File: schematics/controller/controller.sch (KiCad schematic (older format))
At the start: 10 parts

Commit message: PDF render
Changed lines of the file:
@@
 F0 "cpu" 60
 F1 "sub_assy/cpu.sch" 60
+F2 "V_LOGIC" U L 10400 6100 60
+F3 "GND" U L 10400 6200 60
+F4 "SDA_10" B R 12650 5400 60
+F5 "SCL_10" B R 12650 5500 60
+F6 "SDA_HIBAUD" B R 12650 5800 60
+F7 "SCL_HIBAUD" B R 12650 5900 60
+F8 "RESET" I L 10400 5400 60
 $EndSheet
 $EndSCHEMATC

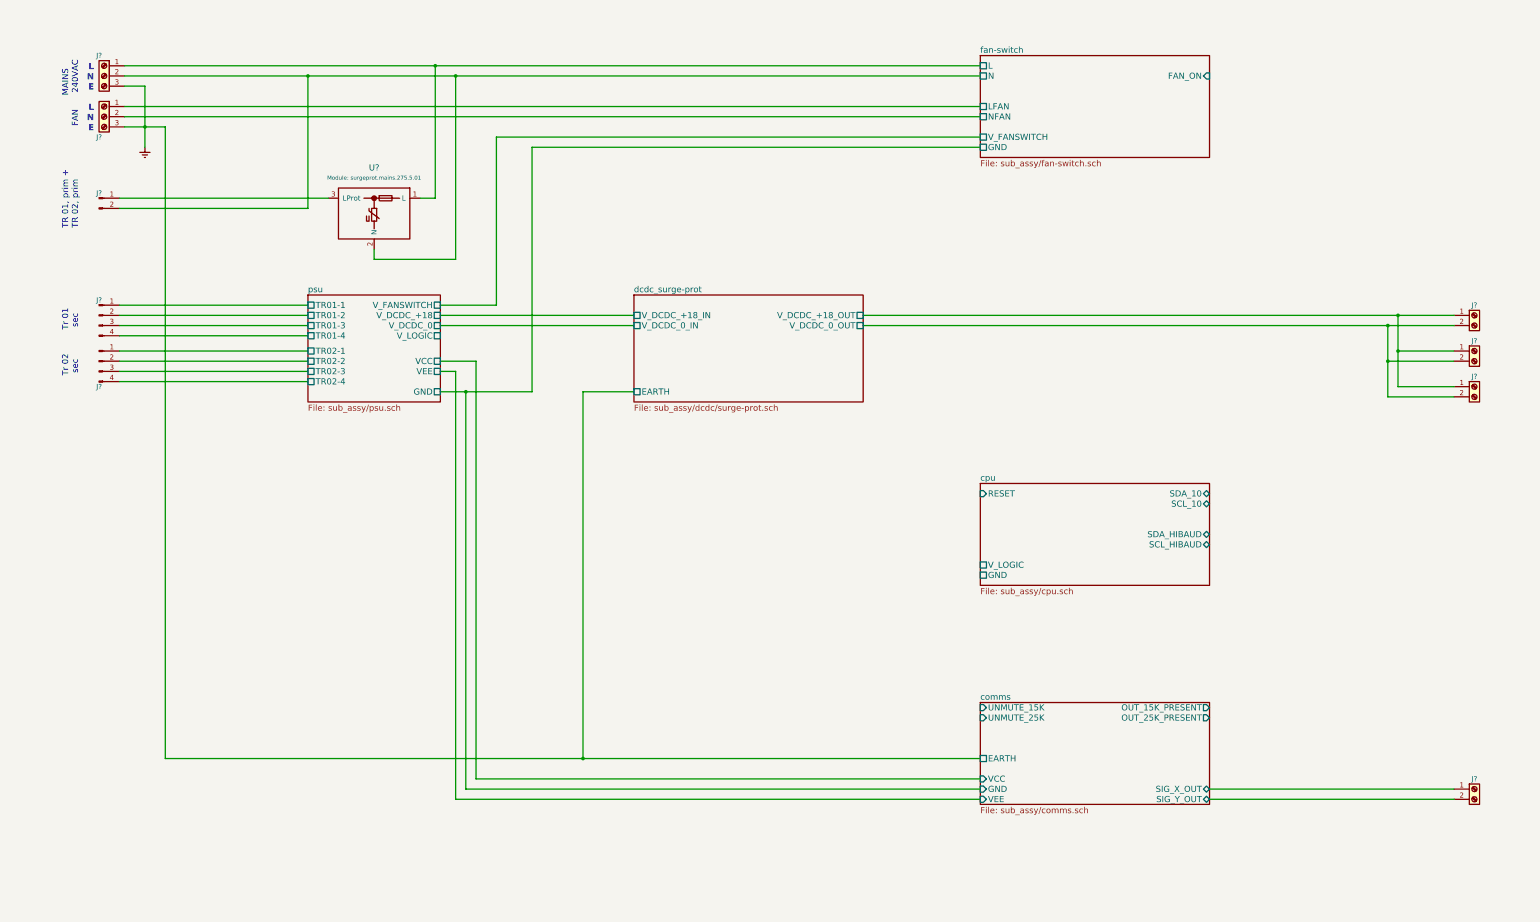
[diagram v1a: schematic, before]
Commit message: Developing and integrating comms i/o router.
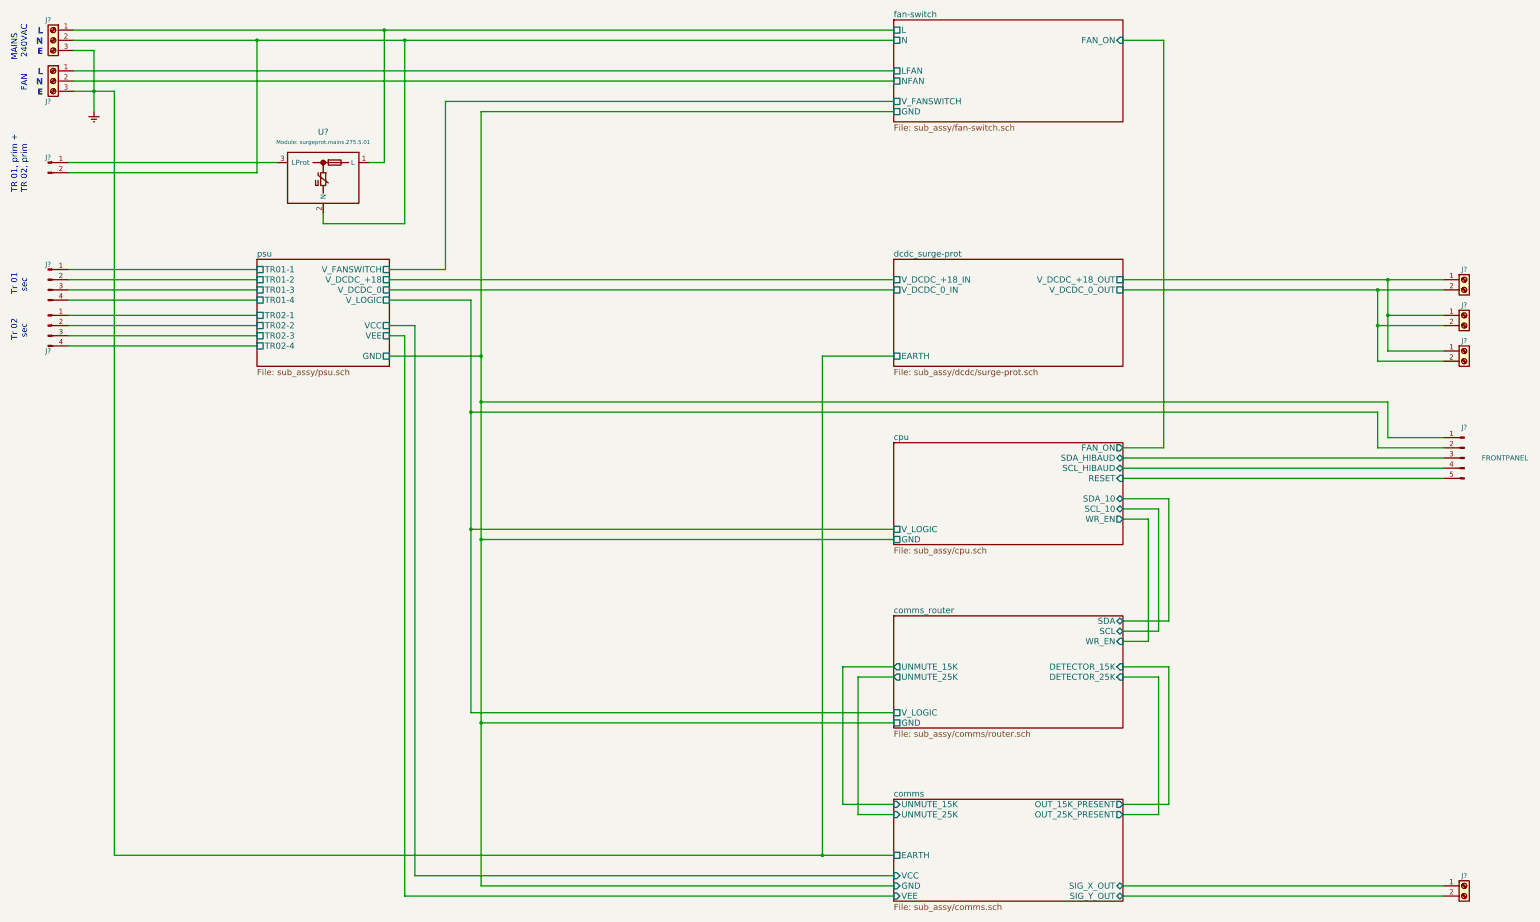
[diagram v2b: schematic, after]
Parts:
- added J?: FRONTPANEL, symbol Conn_01x05_Male
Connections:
- net comms/GND: now also J?.1 (Pin_1)
- net cpu/RESET: now also J?.5 (Pin_5)
- net cpu/SCL_HIBAUD: now also J?.4 (Pin_4)
- net cpu/SDA_HIBAUD: now also J?.3 (Pin_3)
- new net comms_router/V_LOGIC: J?.2 (Pin_2)
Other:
- moved on the sheet: J?, U?

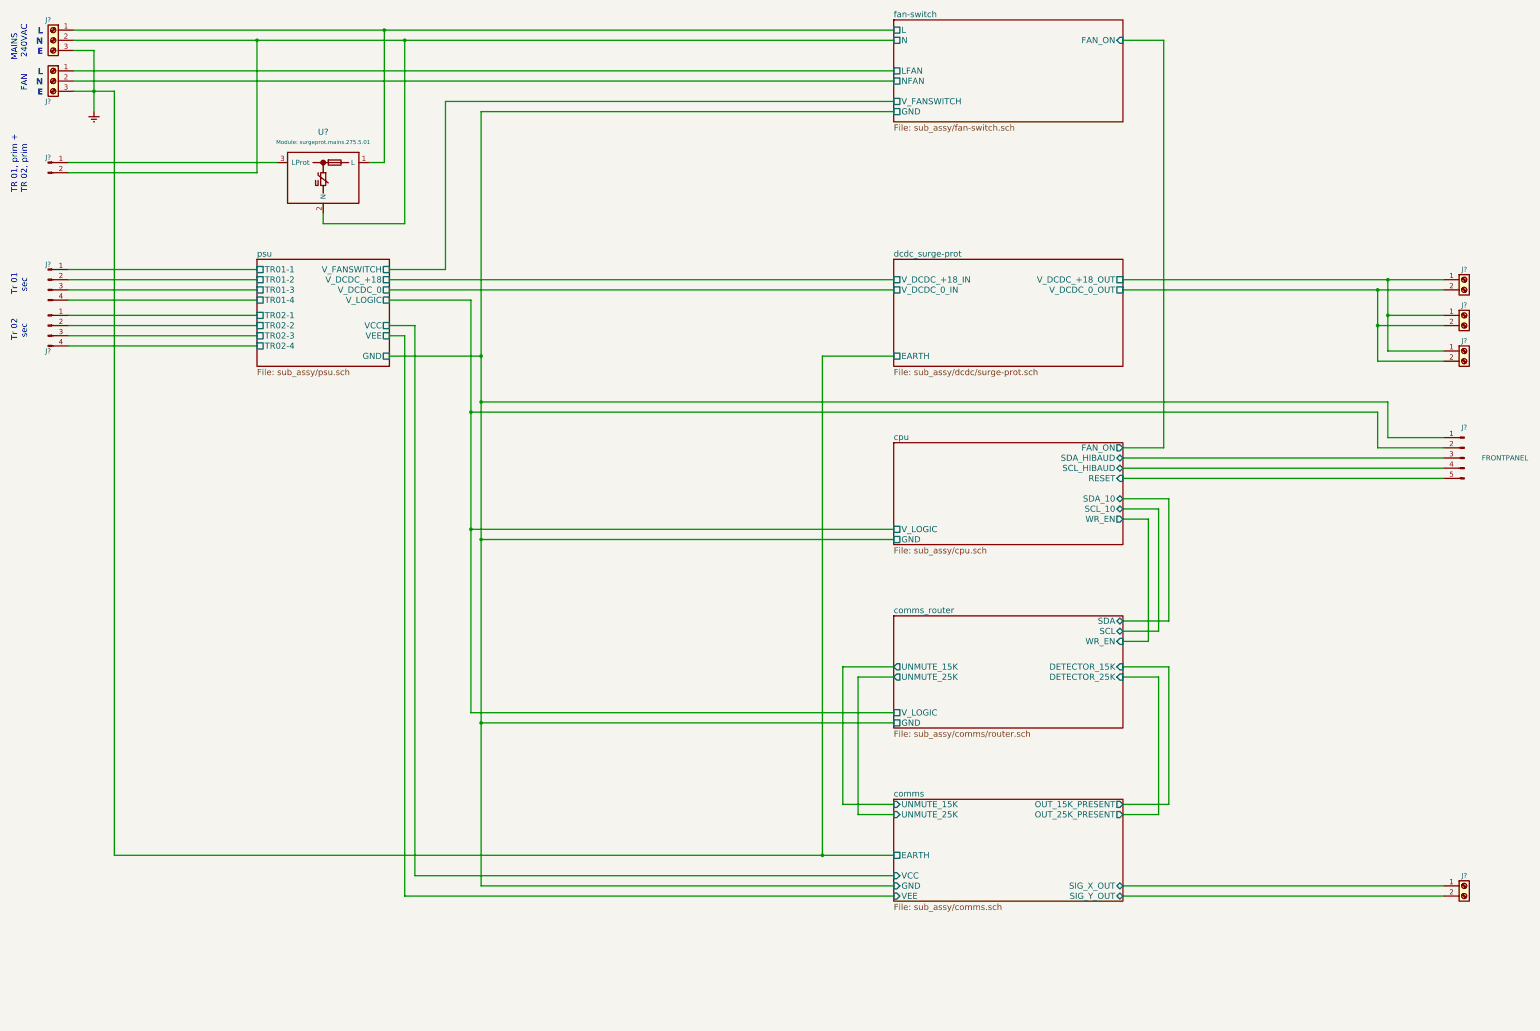
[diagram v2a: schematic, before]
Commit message: Annotation and DRC rule check
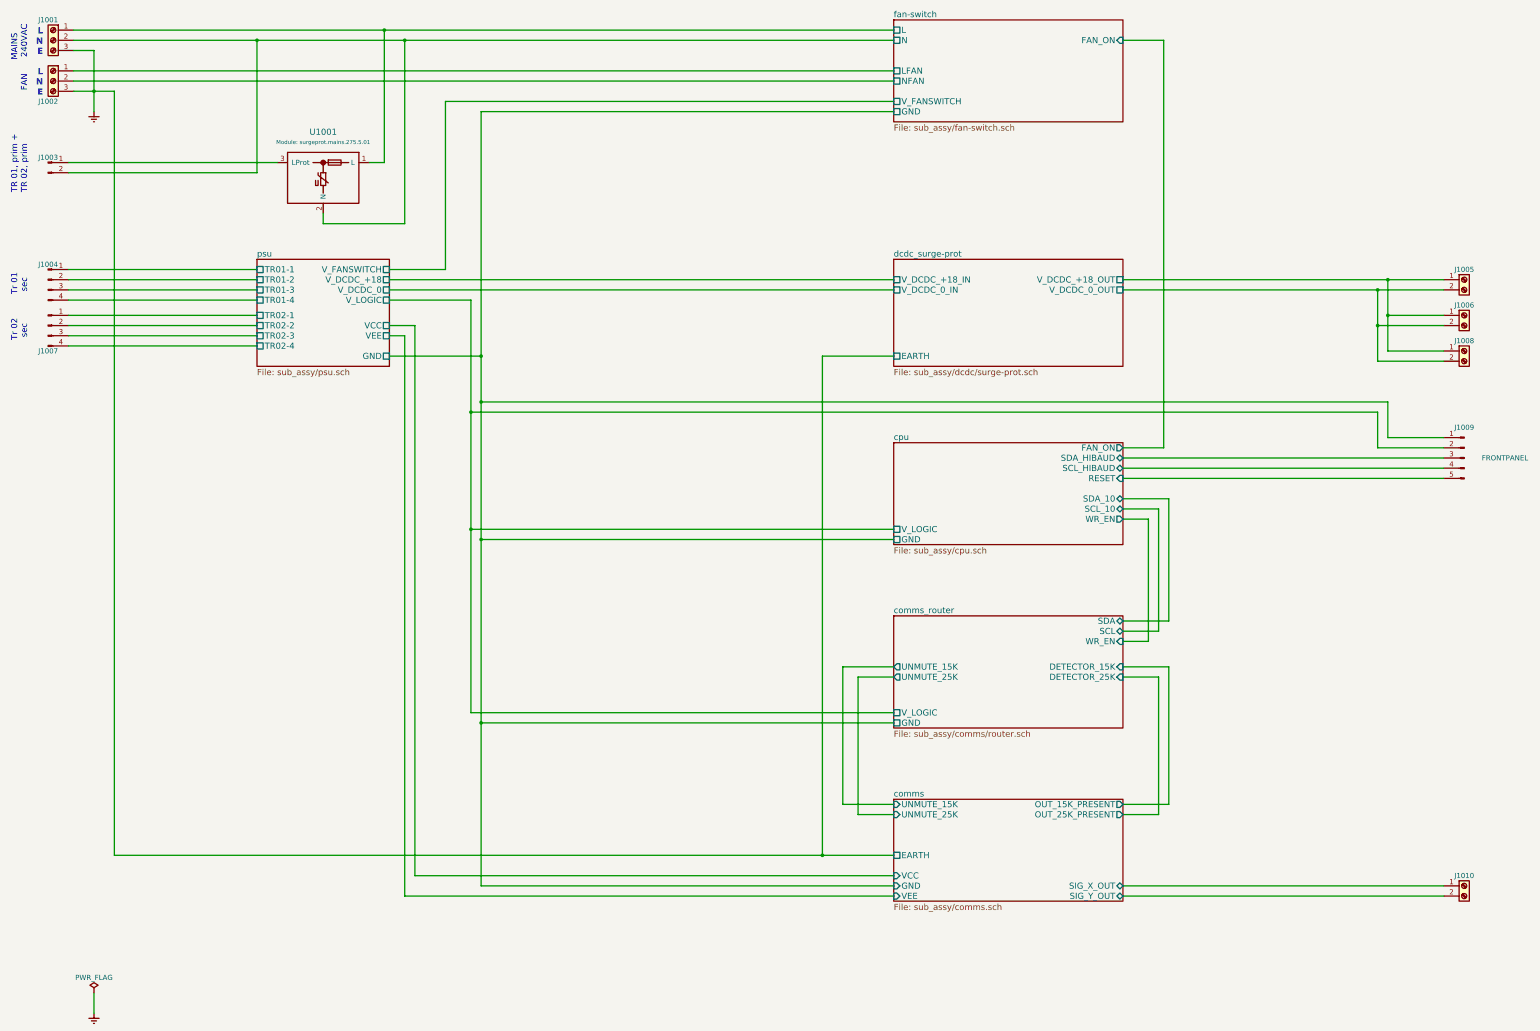
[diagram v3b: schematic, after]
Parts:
- gave numbers to parts that had none: 11
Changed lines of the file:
@@
 $EndSheet
 $Comp
-L Conn_01x04_Male J?
+L Conn_01x04_Male J1004
 U 1 1 59D2E43C
 P 1250 3300
-F 0 "J?" H 1250 3450 50  0000 C CNN
+F 0 "J1004" H 1250 3450 50  0000 C CNN
 F 1 "Conn_01x04_Male" H 1250 3000 50  0001 C CNN
 F 2 "" H 1250 3300 50  0001 C CNN
@@
 $EndComp
 $Comp
-L Conn_01x04_Male J?
+L Conn_01x04_Male J1007
 U 1 1 59D2EA34
 P 1250 3750
-F 0 "J?" H 1250 3500 50  0000 C CNN
+F 0 "J1007" H 1250 3500 50  0000 C CNN
 F 1 "Conn_01x04_Male" H 1250 3450 50  0001 C CNN
 F 2 "" H 1250 3750 50  0001 C CNN
@@
 $EndComp
 $Comp
-L Screw_Terminal_01x03 J?
+L Screw_Terminal_01x03 J1001
 U 1 1 59D41362
 P 1300 950
-F 0 "J?" H 1350 1150 50  0000 C CNN
+F 0 "J1001" H 1350 1150 50  0000 C CNN
 F 1 "Screw_Terminal_01x03" H 1300 750 50  0001 C CNN
 F 2 "" H 1300 950 50  0001 C CNN
@@
 $EndComp
 $Comp
-L Screw_Terminal_01x03 J?
+L Screw_Terminal_01x03 J1002
 U 1 1 59D44A54
 P 1300 1350
-F 0 "J?" H 1350 1150 50  0000 C CNN
+F 0 "J1002" H 1350 1150 50  0000 C CNN
 F 1 "Screw_Terminal_01x03" H 1300 1150 50  0001 C CNN
 F 2 "" H 1300 1350 50  0001 C CNN
@@
 $EndComp
 $Comp
-L Conn_01x02_Male J?
+L Conn_01x02_Male J1003
 U 1 1 59D45F93
 P 1250 2150
-F 0 "J?" H 1250 2200 50  0000 C CNN
+F 0 "J1003" H 1250 2200 50  0000 C CNN
 F 1 "Conn_01x02_Male" H 1250 1950 50  0001 C CNN
 F 2 "" H 1250 2150 50  0001 C CNN
@@
 TR 01, prim +\nTR 02, prim
 $Comp
-L Earth #PWR?
+L Earth #PWR01
 U 1 1 59D4D93F
 P 1700 1650
-F 0 "#PWR?" H 1700 1400 50  0001 C CNN
+F 0 "#PWR01" H 1700 1400 50  0001 C CNN
 F 1 "Earth" H 1700 1500 50  0001 C CNN
 F 2 "" H 1700 1650 50  0001 C CNN
@@
 	1    0    0    -1
 $EndComp
-Wire Wire Line
-	1450 3200 3300 3200
-Wire Wire Line
-	1450 3300 3300 3300
-Wire Wire Line
-	1450 3400 3300 3400
-Wire Wire Line
-	1450 3500 3300 3500
-Wire Wire Line
-	1450 3650 3300 3650
-Wire Wire Line
-	1450 3750 3300 3750
-Wire Wire Line
-	1450 3850 3300 3850
-Wire Wire Line
-	1450 3950 3300 3950
-Wire Wire Line
-	1500 850  9550 850
-Wire Wire Line
-	1500 950  9550 950
-Wire Wire Line
-	1500 1050 1700 1050
-Wire Wire Line
-	1700 1050 1700 1650
-Wire Wire Line
-	1500 1450 1900 1450
-Connection ~ 1700 1450
-$Comp
-L line-protector U?
+$Comp
+L line-protector U1001
 U 1 1 59D3311B
 P 3950 2150
-F 0 "U?" H 3950 2450 60  0000 C CNN
+F 0 "U1001" H 3950 2450 60  0000 C CNN
 F 1 "Module: surgeprot.mains.275.5.01" H 3950 2350 39  0000 C CNN
 F 2 "" H 3950 1800 60  0000 C CNN
@@
 	-1   0    0    -1
 $EndComp
-Wire Wire Line
-	4400 2150 4550 2150
-Wire Wire Line
-	4550 2150 4550 850
-Connection ~ 4550 850
-Wire Wire Line
-	3500 2150 1450 2150
-Wire Wire Line
-	1450 2250 3300 2250
-Wire Wire Line
-	3300 2250 3300 950
-Connection ~ 3300 950
 Text Notes 1050 1150 1    60   ~ 0
   MAINS\n 240VAC
 Text Notes 1050 1450 1    60   ~ 0
 FAN
-Wire Wire Line
-	4600 3200 5150 3200
-Wire Wire Line
-	3950 2650 3950 2750
-Wire Wire Line
-	3950 2750 4750 2750
-Wire Wire Line
-	4750 2750 4750 950
-Connection ~ 4750 950
 Text Notes 1200 900  2    60   ~ 12
 L
@@
 Text Notes 1200 1500 2    60   ~ 12
 E
-Wire Wire Line
-	1500 1250 9550 1250
-Wire Wire Line
-	1500 1350 9550 1350
-Wire Wire Line
-	5150 3200 5150 1550
-Wire Wire Line
-	5150 1550 9550 1550
 $Sheet
 S 9550 8400 2250 1000
@@
 F11 "SIG_Y_OUT" B R 11800 9350 60
 $EndSheet
-Wire Wire Line
-	9550 1650 5500 1650
-Wire Wire Line
-	5500 1650 5500 9250
-Wire Wire Line
-	5500 4050 4600 4050
-$Comp
-L Screw_Terminal_01x02 J?
+$Comp
+L Screw_Terminal_01x02 J1010
 U 1 1 5A4979A3
 P 15150 9250
-F 0 "J?" H 15150 9350 50  0000 C CNN
+F 0 "J1010" H 15150 9350 50  0000 C CNN
 F 1 "Screw_Terminal_01x02" H 15150 9050 50  0001 C CNN
 F 2 "" H 15150 9250 50  0001 C CNN
@@
 	1    0    0    -1
 $EndComp
-Wire Wire Line
-	11800 9250 14950 9250
-Wire Wire Line
-	11800 9350 14950 9350
-Wire Wire Line
-	1900 8950 9550 8950
-Wire Wire Line
-	1900 1450 1900 8950
-Wire Wire Line
-	4600 3850 4750 3850
-Wire Wire Line
-	4750 3850 4750 9350
-Wire Wire Line
-	4750 9350 9550 9350
 $Sheet
 S 9550 3100 2250 1050
@@
 F6 "EARTH" U L 9550 4050 60
 $EndSheet
-Wire Wire Line
-	9550 4050 8850 4050
-Wire Wire Line
-	8850 4050 8850 8950
-Connection ~ 8850 8950
-Wire Wire Line
-	4600 3300 9550 3300
-Wire Wire Line
-	4600 3400 9550 3400
-$Comp
-L Screw_Terminal_01x02 J?
+$Comp
+L Screw_Terminal_01x02 J1005
 U 1 1 5A659D4B
 P 15150 3300
-F 0 "J?" H 15150 3400 50  0000 C CNN
+F 0 "J1005" H 15150 3400 50  0000 C CNN
 F 1 "Screw_Terminal_01x02" H 15150 3100 50  0001 C CNN
 F 2 "" H 15150 3300 50  0001 C CNN
@@
 $EndComp
 $Comp
-L Screw_Terminal_01x02 J?
+L Screw_Terminal_01x02 J1006
 U 1 1 5A659F25
 P 15150 3650
-F 0 "J?" H 15150 3750 50  0000 C CNN
+F 0 "J1006" H 15150 3750 50  0000 C CNN
 F 1 "Screw_Terminal_01x02" H 15150 3450 50  0001 C CNN
 F 2 "" H 15150 3650 50  0001 C CNN
@@
 $EndComp
 $Comp
-L Screw_Terminal_01x02 J?
+L Screw_Terminal_01x02 J1008
 U 1 1 5A65A048
 P 15150 4000
-F 0 "J?" H 15150 4100 50  0000 C CNN
+F 0 "J1008" H 15150 4100 50  0000 C CNN
 F 1 "Screw_Terminal_01x02" H 15150 3800 50  0001 C CNN
 F 2 "" H 15150 4000 50  0001 C CNN
@@
 	1    0    0    -1
 $EndComp
-Wire Wire Line
-	11800 3300 14950 3300
-Wire Wire Line
-	11800 3400 14950 3400
-Wire Wire Line
-	14950 3650 14400 3650
-Wire Wire Line
-	14400 3300 14400 4000
-Connection ~ 14400 3300
-Wire Wire Line
-	14950 3750 14300 3750
-Wire Wire Line
-	14300 3400 14300 4100
-Connection ~ 14300 3400
-Wire Wire Line
-	14400 4000 14950 4000
-Connection ~ 14400 3650
-Wire Wire Line
-	14300 4100 14950 4100
-Connection ~ 14300 3750
 $Sheet
 S 9550 4900 2250 1000
@@
 F10 "GND" U L 9550 7650 60
 $EndSheet
-Wire Wire Line
-	11800 7100 12250 7100
-Wire Wire Line
-	12250 7100 12250 8450
-Wire Wire Line
-	12250 8450 11800 8450
-Wire Wire Line
-	11800 7200 12150 7200
-Wire Wire Line
-	12150 7200 12150 8550
-Wire Wire Line
-	12150 8550 11800 8550
-Wire Wire Line
-	9550 7100 9050 7100
-Wire Wire Line
-	9050 7100 9050 8450
-Wire Wire Line
-	9050 8450 9550 8450
-Wire Wire Line
-	9550 7200 9200 7200
-Wire Wire Line
-	9200 7200 9200 8550
-Wire Wire Line
-	9200 8550 9550 8550
-$Comp
-L Conn_01x05_Male J?
+$Comp
+L Conn_01x05_Male J1009
 U 1 1 5A9D8BFF
 P 15150 5050
-F 0 "J?" H 15150 5350 50  0000 C CNN
+F 0 "J1009" H 15150 5350 50  0000 C CNN
 F 1 "FRONTPANEL" H 14750 5050 50  0000 C CNN
 F 2 "" H 15150 5050 50  0001 C CNN
@@
 	-1   0    0    -1
 $EndComp
+$Comp
+L Earth #PWR02
+U 1 1 5B42110A
+P 1700 10500
+F 0 "#PWR02" H 1700 10250 50  0001 C CNN
+F 1 "Earth" H 1700 10350 50  0001 C CNN
+F 2 "" H 1700 10500 50  0001 C CNN
+F 3 "" H 1700 10500 50  0001 C CNN
+	1    1700 10500
+	1    0    0    -1
+$EndComp
+$Comp
+L PWR_FLAG #FLG03
+U 1 1 5B42127E
+P 1700 10300
+F 0 "#FLG03" H 1700 10375 50  0001 C CNN
+F 1 "PWR_FLAG" H 1700 10450 50  0000 C CNN
+F 2 "" H 1700 10300 50  0001 C CNN
+F 3 "" H 1700 10300 50  0001 C CNN
+	1    1700 10300
+	1    0    0    -1
+$EndComp
+Wire Wire Line
+	1450 3200 3300 3200
+Wire Wire Line
+	1450 3300 3300 3300
+Wire Wire Line
+	1450 3400 3300 3400
+Wire Wire Line
+	1450 3500 3300 3500
+Wire Wire Line
+	1450 3650 3300 3650
+Wire Wire Line
+	1450 3750 3300 3750
+Wire Wire Line
+	1450 3850 3300 3850
+Wire Wire Line
+	1450 3950 3300 3950
+Wire Wire Line
+	1500 850  9550 850
+Wire Wire Line
+	1500 950  9550 950
+Wire Wire Line
+	1500 1050 1700 1050
+Wire Wire Line
+	1700 1050 1700 1650
+Wire Wire Line
+	1500 1450 1900 1450
+Connection ~ 1700 1450
+Wire Wire Line
+	4400 2150 4550 2150
+Wire Wire Line
+	4550 2150 4550 850
+Connection ~ 4550 850
+Wire Wire Line
+	3500 2150 1450 2150
+Wire Wire Line
+	1450 2250 3300 2250
+Wire Wire Line
+	3300 2250 3300 950
+Connection ~ 3300 950
+Wire Wire Line
+	4600 3200 5150 3200
+Wire Wire Line
+	3950 2650 3950 2750
+Wire Wire Line
+	3950 2750 4750 2750
+Wire Wire Line
+	4750 2750 4750 950
+Connection ~ 4750 950
+Wire Wire Line
+	1500 1250 9550 1250
+Wire Wire Line
+	1500 1350 9550 1350
+Wire Wire Line
+	5150 3200 5150 1550
+Wire Wire Line
+	5150 1550 9550 1550
+Wire Wire Line
+	9550 1650 5500 1650
+Wire Wire Line
+	5500 1650 5500 9250
+Wire Wire Line
+	5500 4050 4600 4050
+Wire Wire Line
+	11800 9250 14950 9250
+Wire Wire Line
+	11800 9350 14950 9350
+Wire Wire Line
+	1900 8950 9550 8950
+Wire Wire Line
+	1900 1450 1900 8950
+Wire Wire Line
+	4600 3850 4750 3850
+Wire Wire Line
+	4750 3850 4750 9350
+Wire Wire Line
+	4750 9350 9550 9350
+Wire Wire Line
+	9550 4050 8850 4050
+Wire Wire Line
+	8850 4050 8850 8950
+Connection ~ 8850 8950
+Wire Wire Line
+	4600 3300 9550 3300
+Wire Wire Line
+	4600 3400 9550 3400
+Wire Wire Line
+	11800 3300 14950 3300
+Wire Wire Line
+	11800 3400 14950 3400
+Wire Wire Line
+	14950 3650 14400 3650
+Wire Wire Line
+	14400 3300 14400 4000
+Connection ~ 14400 3300
+Wire Wire Line
+	14950 3750 14300 3750
+Wire Wire Line
+	14300 3400 14300 4100
+Connection ~ 14300 3400
+Wire Wire Line
+	14400 4000 14950 4000
+Connection ~ 14400 3650
+Wire Wire Line
+	14300 4100 14950 4100
+Connection ~ 14300 3750
+Wire Wire Line
+	11800 7100 12250 7100
+Wire Wire Line
+	12250 7100 12250 8450
+Wire Wire Line
+	12250 8450 11800 8450
+Wire Wire Line
+	11800 7200 12150 7200
+Wire Wire Line
+	12150 7200 12150 8550
+Wire Wire Line
+	12150 8550 11800 8550
+Wire Wire Line
+	9550 7100 9050 7100
+Wire Wire Line
+	9050 7100 9050 8450
+Wire Wire Line
+	9050 8450 9550 8450
+Wire Wire Line
+	9550 7200 9200 7200
+Wire Wire Line
+	9200 7200 9200 8550
+Wire Wire Line
+	9200 8550 9550 8550
 Wire Wire Line
 	5500 4500 14400 4500
@@
 Wire Wire Line
 	12050 6850 11800 6850
+Wire Wire Line
+	1700 10500 1700 10300
 $EndSCHEMATC
